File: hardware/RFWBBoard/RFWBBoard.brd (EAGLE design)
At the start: 90 x 56 mm, 55 parts, among them IC1 24LC025ST, J1 CON-71742-2184-BOT, M1 MOUNT-HOLE3.3, M2 MOUNT-HOLE3.3, M3 MOUNT-HOLE3.3, M4 MOUNT-HOLE3.3, U1 MAX2830IPC-7351, U2 LDB212G4010C-001, U3 LDB212G4010C-001, X1 LTI-SASF54GT, X2 LTI-SASF54GT, X3 LTI-SASF54GT, X4 LTI-SASF54GT

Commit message: - Supply under the IC
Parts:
- moved C81 0.50 mm to (35.9, 16.9)
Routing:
- net A3V3: track 365.4 -> 123.3 mm, vias 14 -> 13
- net N$5: track 12.6 -> 10.5 mm
- net N$6: track 7.77 -> 8.15 mm, vias 2 -> 0
- added copper zone on layer 2, net A3V3
- removed copper zone on layer 2, net AGND

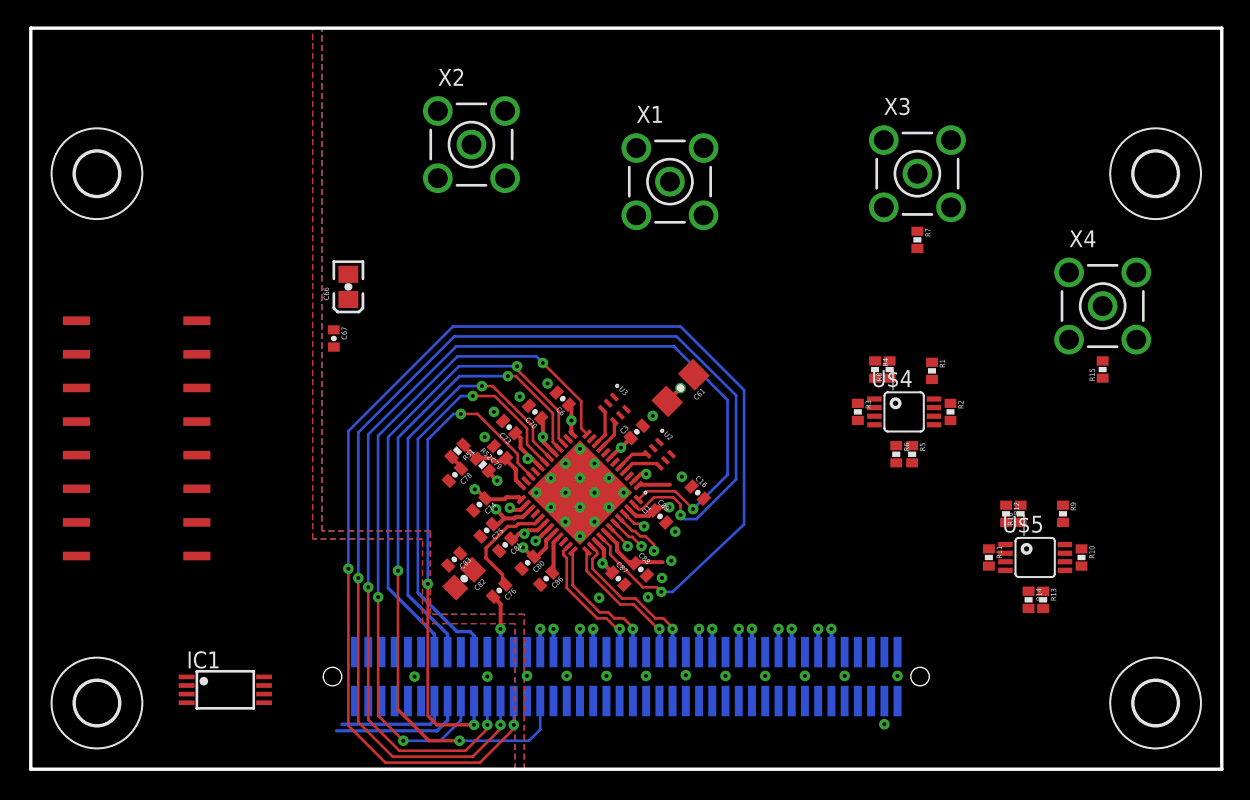
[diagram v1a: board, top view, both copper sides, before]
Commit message: - Routing finished for MAX2830
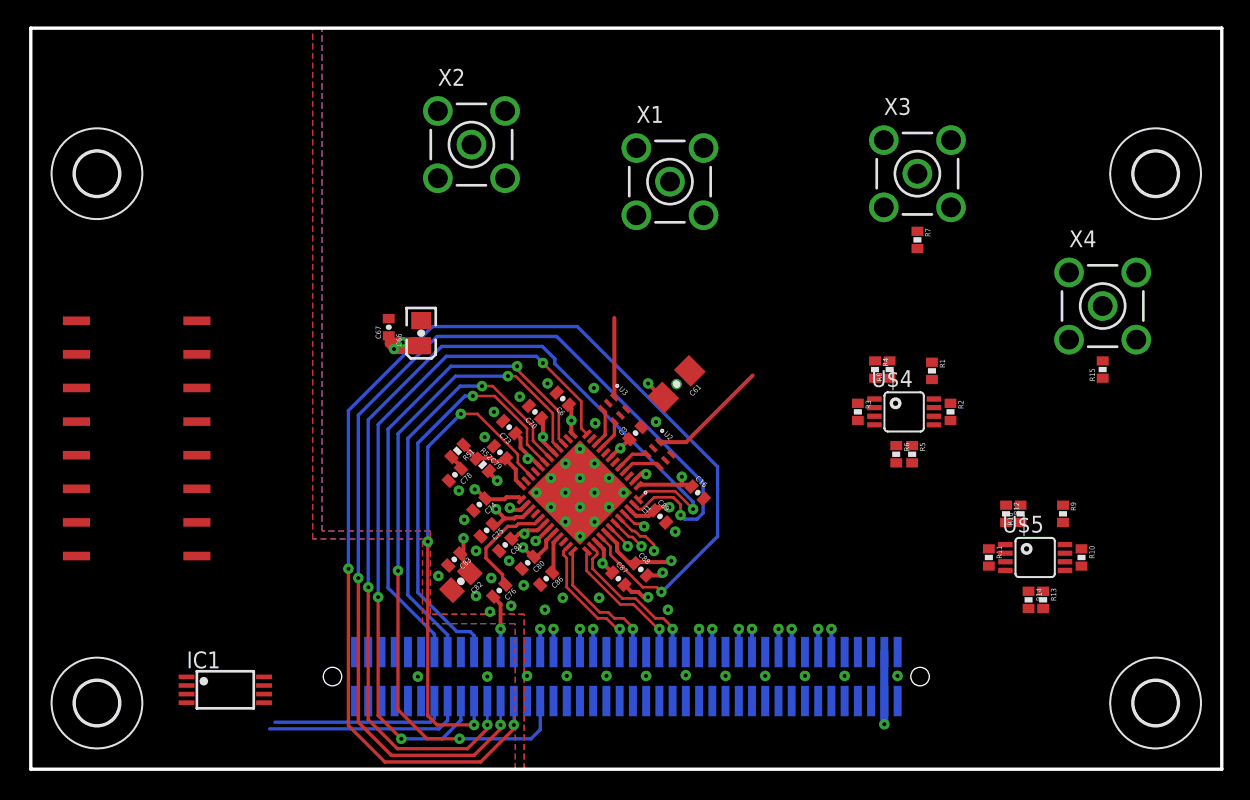
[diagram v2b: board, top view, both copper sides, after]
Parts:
- moved C66 6.52 mm to (29.5, 33.0)
- moved C67 4.24 mm to (27.1, 33.4), turned to 90 degrees
- moved C61 0.42 mm to (48.8, 29.1)
- moved C82 0.32 mm to (32.5, 14.2)
- moved C3 0.14 mm to (45.7, 25.4)
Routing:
- net A3V3: track 123.3 -> 182.9 mm, vias 13 -> 16
- net N$8: track 0.00 -> 9.13 mm
- net GPIO3: track 80.2 -> 72.7 mm
- net GPIO4: track 87.1 -> 80.4 mm
- net N$9: track 0.00 -> 5.98 mm
- net GPIO5: track 99.3 -> 93.4 mm
- net I2C1_SDA: track 10.2 -> 15.2 mm
- net I2C1_SCL: track 8.57 -> 13.5 mm
- net AGND: track 3.84 -> 7.02 mm, vias 38 -> 54

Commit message: - Matched impedance wires for antennas (14 mil -> 50 Ohm) - Baseband for DAC and DAC
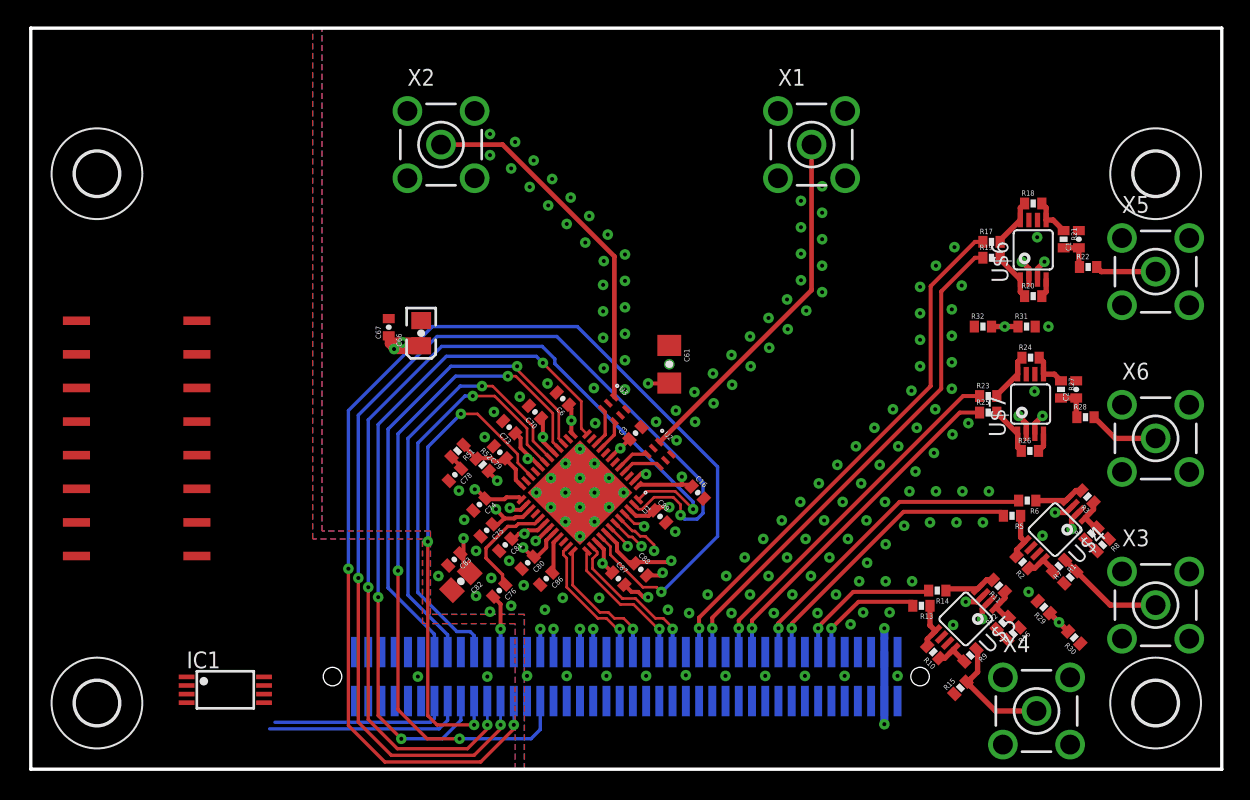
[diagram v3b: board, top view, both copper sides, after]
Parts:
- added C1, C2: 100pF, RFWBBoard:C0402
- added R17, R18, R19, R20, R23, R24, R25, R26: 40k, RFWBBoard:R0402
- added R21, R22, R27, R28: 25, RFWBBoard:R0402
- added R29, R30, R31, R32: 1k, RFWBBoard:R0402
- added U$6, U$7: AD8132MSOP8, RFWBBoard:MSOP8
- added X5, X6: LTI-SASF54GT, RFWBBoard:LTI-SASF54GT
- moved X3 37.2 mm to (85.0, 12.4)
- moved X4 31.0 mm to (76.0, 4.40)
- moved R7 28.0 mm to (78.5, 14.5), turned to 45 degrees
- moved R15 26.3 mm to (70.2, 6.15), turned to 45 degrees
- moved R8 20.9 mm to (81.0, 16.9), turned to 225 degrees
- moved R4 20.5 mm to (80.2, 17.8), turned to 45 degrees
- moved R3 18.5 mm to (79.8, 20.6), turned to 135 degrees
- moved R1 17.6 mm to (77.7, 15.3), turned to 225 degrees
- moved U$4 14.5 mm to (77.4, 18.1), turned to 135 degrees
- moved R10 13.3 mm to (68.2, 8.85), turned to 135 degrees
- moved R9 12.8 mm to (71.0, 8.60), turned to 225 degrees
- moved R2 12.6 mm to (75.0, 15.7), turned to 135 degrees
- moved X1 11.1 mm to (59.0, 47.2)
- moved R6 10.5 mm to (75.3, 20.3), turned to 180 degrees
- moved R13 9.21 mm to (67.3, 12.3), turned to 180 degrees
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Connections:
- new net N$23: R17.2, R18.1, U$6.8
- new net N$24: R19.2, R20.1, U$6.1
- new net N$25: R18.2, R21.1, U$6.5
- new net N$26: R20.2, U$6.4
- new net N$27: C1.1, R21.2, R22.1
- new net N$28: R23.2, R24.1, U$7.8
- new net N$29: R22.2, X5.1
- new net N$30: R25.2, R26.1, U$7.1
- new net N$31: R24.2, R27.1, U$7.5
- new net N$32: R26.2, U$7.4
- new net N$33: C2.1, R27.2, R28.1
- new net N$34: R28.2, X6.1
- new net V_BIAS_ADC: R29.1, R30.2, U$4.2, U$5.2
- new net V_BIAS_DAC: R31.1, R32.2, U$6.2, U$7.2
- net A3V3: now also R29.2, R31.2, U$4.3, U$5.3, U$6.3, U$7.3
- net AGND: now also C1.2, C2.2, R30.1, R32.1, U$4.6, U$5.6, U$6.6, U$7.6, X5.2, X5.3, X5.4, X5.5, X6.2, X6.3, X6.4, X6.5
- net DAC1+: now also R19.1
- net DAC1-: now also R17.1
- net DAC2+: now also R25.1
- net DAC2-: now also R23.1
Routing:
- net A3V3: track 182.9 -> 245.7 mm, vias 16 -> 23
- net DAC1-: track 1.75 -> 40.2 mm
- net DAC1+: track 1.75 -> 38.6 mm
- net DAC2-: track 1.75 -> 27.6 mm
- net DAC2+: track 1.75 -> 26.1 mm
- net ADC1-: track 1.75 -> 23.9 mm
- net N$9: track 5.98 -> 27.2 mm
- net ADC1+: track 1.75 -> 21.5 mm
- net V_BIAS_ADC: track 0.00 -> 18.4 mm, vias 0 -> 3
- net N$8: track 9.13 -> 27.2 mm
- net V_BIAS_DAC: track 0.00 -> 17.7 mm, vias 0 -> 3
- net ADC2-: track 1.75 -> 11.2 mm
- net N$16: track 0.00 -> 8.81 mm
- net N$11: track 0.00 -> 8.25 mm
- net ADC2+: track 1.75 -> 8.76 mm
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
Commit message: - Routing done for RF board
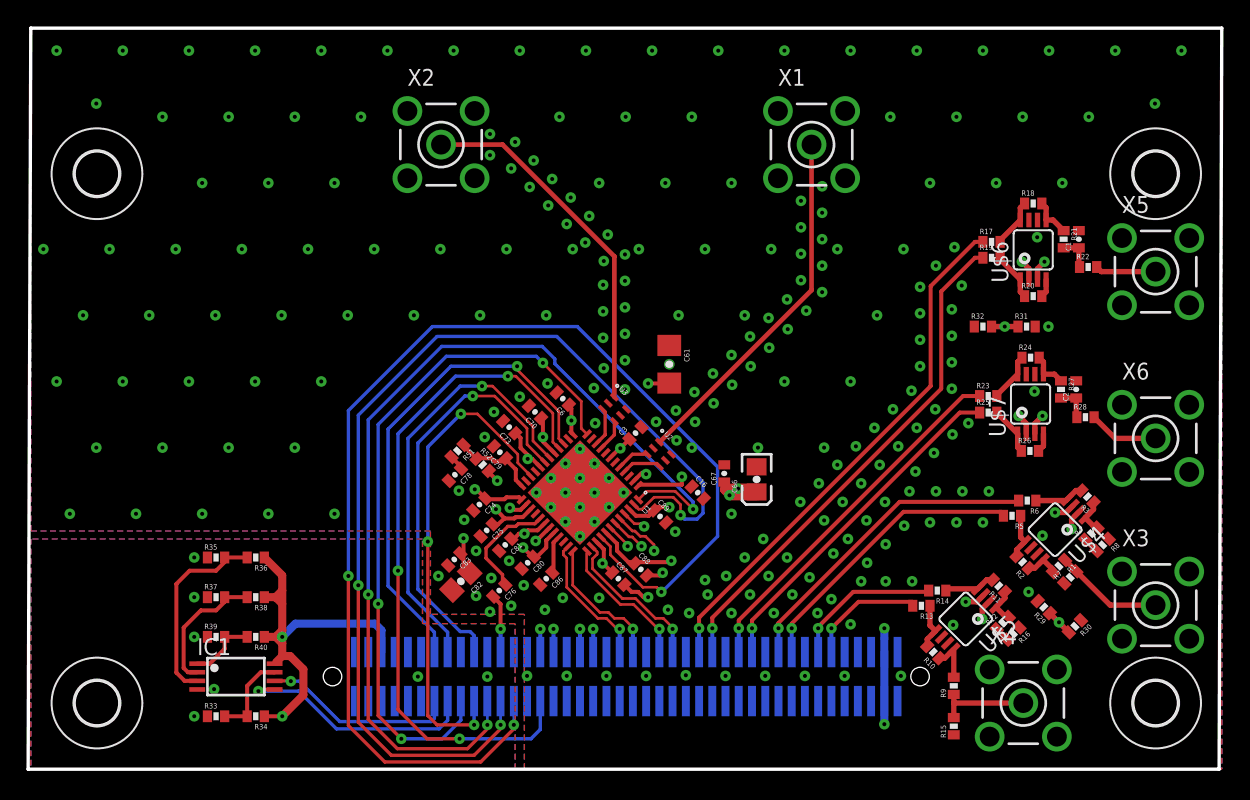
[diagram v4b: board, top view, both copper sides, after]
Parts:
- removed U$3: 204-214-SWITCH, RFWBBoard:204-DIP-SWITCH-FOOTPRINT
- added R33, R34, R35, R36, R37, R38, R39, R40: NONE, RFWBBoard:R0402
- R29, R30, R31, R32: value 1k -> 10k
- moved C66 27.7 mm to (54.9, 21.9)
- moved C67 27.7 mm to (52.4, 22.4)
- moved R15 2.94 mm to (69.8, 3.25), turned to 90 degrees
- moved R9 2.62 mm to (69.8, 6.30), turned to 90 degrees
- moved IC1 1.28 mm to (15.5, 7.00)
- moved X4 1.17 mm to (75.0, 5.00)
- moved R30 0.85 mm to (78.9, 10.8), turned to 225 degrees
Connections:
- net A0: now also R39.2, R40.2; no longer U$3.10, U$3.9
- net A1: now also R37.2, R38.2; no longer U$3.11, U$3.12
- net A2: now also R35.2, R36.2; no longer U$3.13, U$3.14
- net D3V3: now also R34.1, R36.1, R38.1, R40.1; no longer U$3.2, U$3.4, U$3.6, U$3.8
- net DGND: now also R33.1, R35.1, R37.1, R39.1; no longer U$3.1, U$3.3, U$3.5, U$3.7
- net WP: now also R33.2, R34.2; no longer U$3.15, U$3.16
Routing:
- net A3V3: track 245.7 -> 189.3 mm
- net D3V3: track 0.00 -> 30.5 mm, vias 0 -> 2
- net A2: track 0.00 -> 14.9 mm
- net A1: track 0.00 -> 10.2 mm
- net WP: track 0.00 -> 6.60 mm
- net A0: track 0.00 -> 5.14 mm
- net I2C1_SDA: track 15.2 -> 18.5 mm, vias 0 -> 1
- net N$16: track 8.81 -> 7.13 mm
- net I2C1_SCL: track 13.5 -> 14.8 mm, vias 0 -> 1
- net N$20: track 2.63 -> 3.35 mm
- net AGND: vias 171 -> 253
- added copper zone on layer 2, net AGND
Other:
- board size 90 x 56 mm -> 90.2 x 56 mm

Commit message: RF board - schematic cleaned up - component names changed - routing done - silk screen done - logos still missing
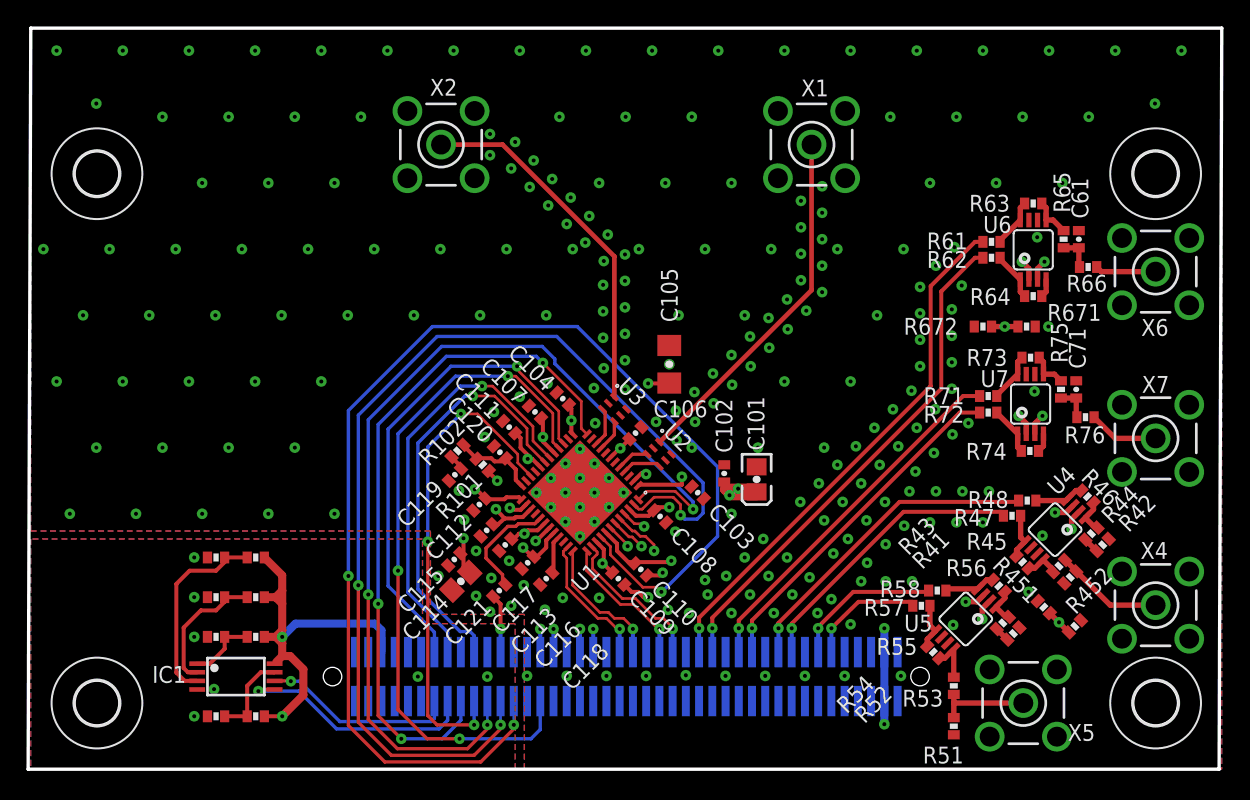
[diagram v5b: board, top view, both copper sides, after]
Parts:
- removed C1: 100pF, RFWBBoard:C0402
- removed R15: 50, RFWBBoard:R0402
- removed R16: 25, RFWBBoard:R0402
- removed X3: LTI-SASF54GT, RFWBBoard:LTI-SASF54GT
- added C105: 10uF, RFWBBoard:C1206
- added R101: 750, RFWBBoard:R0402
- added R102: 1.2k, RFWBBoard:R0402
- added X7: LTI-SASF54GT, RFWBBoard:LTI-SASF54GT
- C61: value 10uF -> 100pF; device RFWBBoard:C1206 -> RFWBBoard:C0402
- R51: value 1.2k -> 50
- R52: value 750 -> 25
- moved R51 42.9 mm to (69.8, 3.25), turned to 90 degrees
- moved R52 42.1 mm to (74.2, 10.2), turned to 225 degrees
- moved X5 34.1 mm to (75.0, 5.00)
- moved C61 32.4 mm to (79.2, 40.0), turned to 90 degrees
- moved X6 12.6 mm to (85.0, 37.6)
- moved X4 12.4 mm to (85.0, 12.4)
- turned C106 to 225 degrees
- renumbered C16 to C103, C2 to C71, C3 to C106, C6 to C104, C66 to C101, C67 to C102, C70 to C107, C73 to C111, C74 to C112, C75 to C113, C76 to C121, C78 to C119, C79 to C120, C80 to C118, C81 to C116, C82 to C114, C83 to C115, C86 to C117, C87 to C109, C88 to C110, C89 to C108, R1 to R43, R10 to R55, R11 to R56, R12 to R54, R13 to R57, R14 to R58, R17 to R61, R18 to R63, R19 to R62, R2 to R45, R20 to R64, R21 to R65, R22 to R66, R23 to R71, R24 to R73, R25 to R72, R26 to R74, R27 to R75, R28 to R76, R29 to R451, R3 to R46, R30 to R452, R31 to R671, R32 to R672, R33 to RWP0, R34 to RWP1, R35 to RA20, R36 to RA21, R37 to RA10, R38 to RA11, R39 to RA00, R4 to R44, R40 to RA01, R5 to R47, R6 to R48, R7 to R41, R8 to R42, R9 to R53, U$4 to U4, U$5 to U5, U$6 to U6, U$7 to U7
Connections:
- net A3V3: now also C105.2, C106.2; no longer C106.1, C61.2
- net AGND: now also C105.1, C106.1, C61.2, R51.1, R52.1, X7.2, X7.3, X7.4, X7.5; no longer C1.2, C106.2, C61.1, R15.1, R16.1, X3.2, X3.3, X3.4, X3.5
- net N$10: now also R101.1, R102.1; no longer R51.1, R52.1
- net N$11: now also X4.1; no longer X3.1
- net N$16: now also R51.2, X5.1; no longer R15.2, X4.1
- net N$22: now also R52.2; no longer R16.2
- net N$27: now also C61.1; no longer C1.1
- net N$29: now also X6.1; no longer X5.1
- net N$34: now also X7.1; no longer X6.1
- net N$5: now also R101.2; no longer R52.2
- net N$7: now also R102.2; no longer R51.2
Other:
- board text added: "0"
- board text added: "1"
- board text added: "2.4 GHz"
- board text added: "A0"
- board text added: "A1"
- board text added: "A2"
- board text added: "ADC1"
- board text added: "ADC2"
- board text added: "Base Band"
- board text added: "DAC1"
- board text added: "DAC2"
- board text added: "EEPROM"
- board text added: "EEPROM I2C"
- board text added: "RX"
- board text added: "TX"
- board text added: "address setup"
- board text added: "protection"
- board text added: "write"

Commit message: - Some GND vias added...
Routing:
- net AGND: vias 253 -> 257
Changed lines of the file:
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@@
 <layer number="20" name="Dimension" color="15" fill="1" visible="yes" active="yes"/>
 <layer number="21" name="tPlace" color="7" fill="1" visible="yes" active="yes"/>
-<layer number="22" name="bPlace" color="7" fill="1" visible="no" active="yes"/>
+<layer number="22" name="bPlace" color="7" fill="1" visible="yes" active="yes"/>
 <layer number="23" name="tOrigins" color="15" fill="1" visible="yes" active="yes"/>
 <layer number="24" name="bOrigins" color="15" fill="1" visible="yes" active="yes"/>
@@
 <layer number="43" name="vRestrict" color="2" fill="10" visible="no" active="yes"/>
 <layer number="44" name="Drills" color="7" fill="1" visible="no" active="yes"/>
-<layer number="45" name="Holes" color="7" fill="1" visible="no" active="yes"/>
+<layer number="45" name="Holes" color="7" fill="1" visible="yes" active="yes"/>
 <layer number="46" name="Milling" color="3" fill="1" visible="no" active="yes"/>
 <layer number="47" name="Measures" color="7" fill="1" visible="no" active="yes"/>
@@
 <contactref element="C105" pad="1"/>
 <contactref element="C106" pad="1"/>
+<via x="42.95" y="2.3" extent="1-16" drill="0.3"/>
+<via x="47.95" y="2.3" extent="1-16" drill="0.3"/>
+<via x="52.95" y="2.3" extent="1-16" drill="0.3"/>
+<via x="57.95" y="2.3" extent="1-16" drill="0.3"/>
 <wire x1="41.5" y1="19.8" x2="41.5" y2="20.9" width="0" layer="19" extent="1-1"/>
 </signal>
@@
 <wire x1="64.5" y1="3.4" x2="64.5" y2="10.65" width="1.27" layer="3"/>
 <contactref element="C106" pad="2"/>
+<wire x1="45.240378125" y1="24.940378125" x2="44.55" y2="24.25" width="0.3048" layer="1"/>
 <wire x1="76.9" y1="33.45" x2="75.9" y2="33.45" width="0" layer="19" extent="1-3"/>
 <wire x1="78" y1="36.95" x2="77.9" y2="34.45" width="0" layer="19" extent="3-3"/>
@@
 <wire x1="64.5" y1="5.15" x2="64.5" y2="3.4" width="0" layer="19" extent="2-16"/>
 <wire x1="77.8" y1="25.35" x2="78" y2="22" width="0" layer="19" extent="3-3"/>
-<wire x1="45.240378125" y1="24.940378125" x2="44.55" y2="24.25" width="0.3048" layer="1"/>
 </signal>
 <signal name="ARESERVED">
